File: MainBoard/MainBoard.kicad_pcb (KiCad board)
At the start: 2 copper layers, 55 x 50 mm, 18 parts, among them CN1 HC-FPC-05-09-22RLTAG, CN3 PJ-342, J1 1769, Q2 MMBT2222ALT1G, U1 V3S, U10 F35SQA512M-WWT, U11 XC6206P302MR_C5148691, U2 ESP32-MINI-1-H4, U3 SGTL5000XNAA3R2, U4 BQ27220YZFR, U5 10104110-0001LF, U6 EA3036C, U7 MT3608, U8 PCM1807PW, U9 BQ24074RGTR, X1 FC-12M32.768KHZ7PF20PPM, X2 X322524MOB4SI

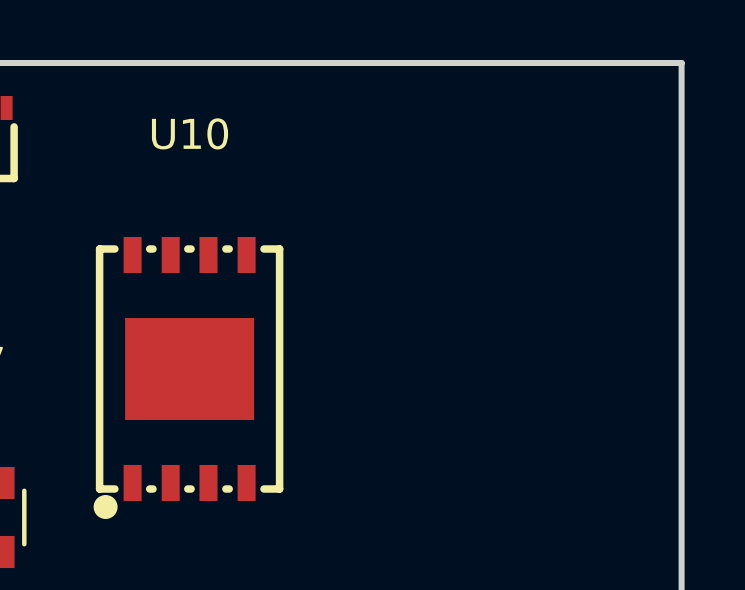
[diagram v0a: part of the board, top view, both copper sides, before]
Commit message: footprints for wheel + power changes for v3s
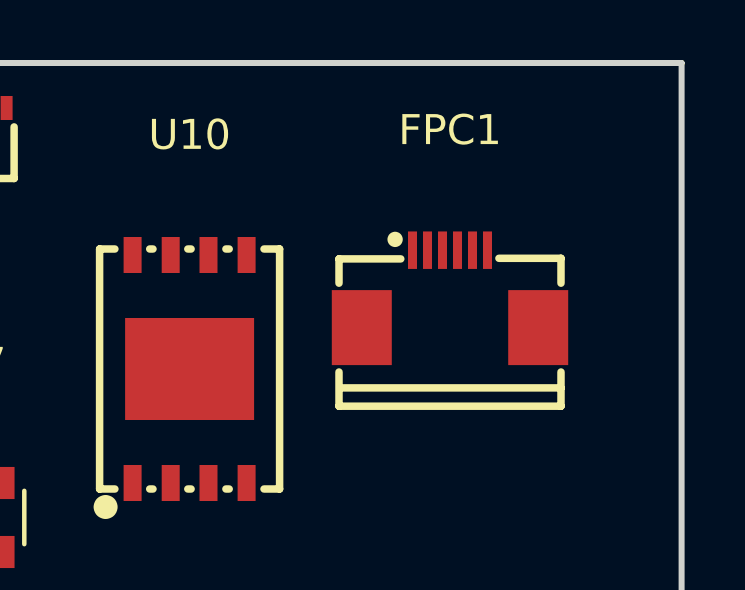
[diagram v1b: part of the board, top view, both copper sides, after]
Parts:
- added FPC1: FPC-05F-6PH20, easyeda2kicad:FPC-SMD_6P-P0.50_XUNPU_FPC-05F-6PH20, F.Cu at (169.8, 82.5)

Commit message: minor power changes
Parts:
- added C1: 10uF, Capacitor_SMD:C_0603_1608Metric, F.Cu at (182.2, 78.2)
- added C10: 220pF, Capacitor_SMD:C_0402_1005Metric, F.Cu at (181.6, 95.8)
- added C11: 220uF, Capacitor_SMD:C_1206_3216Metric, F.Cu at (203.7, 92.4)
- added C12: 220uF, Capacitor_SMD:C_1206_3216Metric, F.Cu at (203.7, 95.8)
- added C13: 1uF, Capacitor_SMD:C_0402_1005Metric, F.Cu at (202.3, 98.4)
- added C14: 1uF, Capacitor_SMD:C_0402_1005Metric, F.Cu at (202.3, 100.4)
- added C15: 0.1uF, Capacitor_SMD:C_0402_1005Metric, F.Cu at (198.3, 77.9)
- added C16: 0.1uF, Capacitor_SMD:C_0402_1005Metric, F.Cu at (202.3, 102.4)
- added C17: 10uF, Capacitor_SMD:C_0603_1608Metric, F.Cu at (186.2, 80.7)
- added C18: 0.1uF, Capacitor_SMD:C_0402_1005Metric, F.Cu at (205.1, 98.4)
- added C19: 0.1uF, Capacitor_SMD:C_0402_1005Metric, F.Cu at (181.6, 97.8)
- added C2: 10uF, Capacitor_SMD:C_0603_1608Metric, F.Cu at (182.2, 80.7)
- added C20: 0.1uF, Capacitor_SMD:C_0402_1005Metric, F.Cu at (205.1, 100.4)
- added C21: 0.1uF, Capacitor_SMD:C_0402_1005Metric, F.Cu at (205.1, 102.4)
- added C22: 0.1uF, Capacitor_SMD:C_0402_1005Metric, F.Cu at (208.0, 98.4)
- added C23: 0.1uF, Capacitor_SMD:C_0402_1005Metric, F.Cu at (208.0, 100.4)
- added C24: 0.1uF, Capacitor_SMD:C_0402_1005Metric, F.Cu at (208.0, 102.4)
- added C25: 1uF, Capacitor_SMD:C_0402_1005Metric, F.Cu at (181.6, 99.8)
- added C26: 4.7uF, Capacitor_SMD:C_0402_1005Metric, F.Cu at (181.6, 101.7)
- added C27: 4.7uF, Capacitor_SMD:C_0402_1005Metric, F.Cu at (184.5, 87.9)
- added C28: 22uF, Capacitor_SMD:C_0603_1608Metric, F.Cu at (186.2, 83.2)
- added C29: 22uF, Capacitor_SMD:C_0603_1608Metric, F.Cu at (186.2, 85.7)
- added C3: 10uF, Capacitor_SMD:C_0603_1608Metric, F.Cu at (182.2, 83.2)
- added C30: 0.1uF, Capacitor_SMD:C_0402_1005Metric, F.Cu at (212.9, 91.7)
- added C31: 0.1uF, Capacitor_SMD:C_0402_1005Metric, F.Cu at (212.9, 93.7)
- added C32: 1uF, Capacitor_SMD:C_0402_1005Metric, F.Cu at (212.9, 95.7)
- added C33: 0.1uF, Capacitor_SMD:C_0402_1005Metric, F.Cu at (212.9, 97.6)
- added C34: 0.1uF, Capacitor_SMD:C_0402_1005Metric, F.Cu at (198.3, 79.9)
- added C35: 0.1uF, Capacitor_SMD:C_0402_1005Metric, F.Cu at (212.9, 101.6)
- added C36: 0.1uF, Capacitor_SMD:C_0402_1005Metric, F.Cu at (198.3, 81.8)
- added C37: 0.1uF, Capacitor_SMD:C_0402_1005Metric, F.Cu at (198.3, 83.8)
- added C38: 15pF, Capacitor_SMD:C_0402_1005Metric, F.Cu at (198.3, 85.8)
- added C39: 15pF, Capacitor_SMD:C_0402_1005Metric, F.Cu at (198.3, 87.8)
- added C4: 1uF, Capacitor_SMD:C_0402_1005Metric, F.Cu at (181.6, 87.9)
- added C40: 1.0uF, Capacitor_SMD:C_0402_1005Metric, F.Cu at (184.5, 89.9)
- added C41: 1.0uF, Capacitor_SMD:C_0402_1005Metric, F.Cu at (184.5, 91.9)
- added C42: 0.1uF, Capacitor_SMD:C_0402_1005Metric, F.Cu at (201.1, 77.9)
- added C43: 18pF, Capacitor_SMD:C_0402_1005Metric, F.Cu at (201.1, 79.9)
- added C44: 0.1uF, Capacitor_SMD:C_0402_1005Metric, F.Cu at (201.1, 81.8)
- added C45: 10uF, Capacitor_SMD:C_0603_1608Metric, F.Cu at (207.4, 78.2)
- added C46: 4.7uF, Capacitor_SMD:C_0402_1005Metric, F.Cu at (201.1, 83.8)
- added C47: 0.1uF, Capacitor_SMD:C_0402_1005Metric, F.Cu at (201.1, 85.8)
- added C48: 0.1uF, Capacitor_SMD:C_0402_1005Metric, F.Cu at (201.1, 87.8)
- added C49: 18pF, Capacitor_SMD:C_0402_1005Metric, F.Cu at (204.0, 77.9)
- added C5: 220pF, Capacitor_SMD:C_0402_1005Metric, F.Cu at (181.6, 89.9)
- added C50: 2.2uF, Capacitor_SMD:C_0402_1005Metric, F.Cu at (184.5, 93.8)
- added C51: 1uF, Capacitor_SMD:C_0402_1005Metric, F.Cu at (184.5, 95.8)
- added C52: 10uF, Capacitor_SMD:C_0603_1608Metric, F.Cu at (198.8, 92.0)
- added C53: 10uF, Capacitor_SMD:C_0603_1608Metric, F.Cu at (198.8, 94.5)
- added C54: 10uF, Capacitor_SMD:C_0603_1608Metric, F.Cu at (198.8, 97.0)
- added C55: 0.1uF, Capacitor_SMD:C_0402_1005Metric, F.Cu at (184.5, 97.8)
- added C56: 0.1uF, Capacitor_SMD:C_0402_1005Metric, F.Cu at (184.5, 99.8)
- added C57: 0.1uF, Capacitor_SMD:C_0402_1005Metric, F.Cu at (184.5, 101.7)
- added C58: 10uF, Capacitor_SMD:C_0603_1608Metric, F.Cu at (190.2, 78.2)
- added C59: 0.1uF, Capacitor_SMD:C_0402_1005Metric, F.Cu at (187.4, 87.9)
- added C6: 10uF, Capacitor_SMD:C_0603_1608Metric, F.Cu at (182.2, 85.7)
- added C60: 0.1uF, Capacitor_SMD:C_0402_1005Metric, F.Cu at (187.4, 89.9)
- added C61: 0.1uF, Capacitor_SMD:C_0402_1005Metric, F.Cu at (187.4, 91.9)
- added C62: 10uF, Capacitor_SMD:C_0603_1608Metric, F.Cu at (190.2, 80.7)
- added C63: 0.1uF, Capacitor_SMD:C_0402_1005Metric, F.Cu at (187.4, 93.8)
- added C64: 0.1uF, Capacitor_SMD:C_0402_1005Metric, F.Cu at (187.4, 95.8)
- added C65: 0.1uF, Capacitor_SMD:C_0402_1005Metric, F.Cu at (187.4, 97.8)
- added C66: 10uF, Capacitor_SMD:C_0603_1608Metric, F.Cu at (190.2, 83.2)
- added C67: 0.1uF, Capacitor_SMD:C_0402_1005Metric, F.Cu at (187.4, 99.8)
- added C68: 0.1uF, Capacitor_SMD:C_0402_1005Metric, F.Cu at (187.4, 101.7)
- added C69: 0.1uF, Capacitor_SMD:C_0402_1005Metric, F.Cu at (190.2, 87.9)
- added C7: 10uF, Capacitor_SMD:C_0603_1608Metric, F.Cu at (186.2, 78.2)
- added C70: 0.1uF, Capacitor_SMD:C_0402_1005Metric, F.Cu at (190.2, 89.9)
- added C71: 0.1uF, Capacitor_SMD:C_0402_1005Metric, F.Cu at (190.2, 91.9)
- added C72: 0.1uF, Capacitor_SMD:C_0402_1005Metric, F.Cu at (190.2, 93.8)
- added C73: 0.1uF, Capacitor_SMD:C_0402_1005Metric, F.Cu at (190.2, 95.8)
- added C74: 0.1uF, Capacitor_SMD:C_0402_1005Metric, F.Cu at (190.2, 97.8)
- added C75: 0.1uF, Capacitor_SMD:C_0402_1005Metric, F.Cu at (204.0, 79.9)
- added C76: 10uF, Capacitor_SMD:C_0603_1608Metric, F.Cu at (190.2, 85.7)
- added C77: 0.1uF, Capacitor_SMD:C_0402_1005Metric, F.Cu at (190.2, 99.8)
- added C78: 10uF, Capacitor_SMD:C_0603_1608Metric, F.Cu at (207.4, 80.7)
- added C79: 0.1uF, Capacitor_SMD:C_0402_1005Metric, F.Cu at (204.0, 81.8)
- added C8: 220pF, Capacitor_SMD:C_0402_1005Metric, F.Cu at (181.6, 91.9)
- added C9: 10uF, Capacitor_SMD:C_0402_1005Metric, F.Cu at (181.6, 93.8)
- added D1: RED, LED_SMD:LED_0402_1005Metric, F.Cu at (193.4, 88.0)
- added D2: GREEN, LED_SMD:LED_0402_1005Metric, F.Cu at (193.4, 89.9)
- added D3: D, Diode_SMD:D_0603_1608Metric, F.Cu at (195.3, 117.6)
- added H1: MountingHole, MountingHole:MountingHole_2.2mm_M2, F.Cu at (175.0, 77.5)
- added H2: MountingHole, MountingHole:MountingHole_2.2mm_M2, F.Cu at (140.0, 77.5)
- added H3: MountingHole, MountingHole:MountingHole_2.2mm_M2, F.Cu at (160.0, 122.5)
- added H4: MountingHole, MountingHole:MountingHole_2.2mm_M2, F.Cu at (125.0, 107.5)
- added JP1: SolderJumper_2_Open, Jumper:SolderJumper-2_P1.3mm_Open_Pad1.0x1.5mm, F.Cu at (185.8, 110.3)
- added JP2: SolderJumper_2_Open, Jumper:SolderJumper-2_P1.3mm_Open_Pad1.0x1.5mm, F.Cu at (185.8, 113.8)
- added JP3: SolderJumper_2_Open, Jumper:SolderJumper-2_P1.3mm_Open_Pad1.0x1.5mm, F.Cu at (182.2, 118.4)
- added L1: 1.5uH, Inductor_SMD:L_0402_1005Metric, F.Cu at (193.1, 91.9)
- added L2: 1.5uH, Inductor_SMD:L_0402_1005Metric, F.Cu at (193.1, 93.9)
- added L3: 1.5uH, Inductor_SMD:L_0402_1005Metric, F.Cu at (193.1, 95.9)
- added L4: 4.7uH, Inductor_SMD:L_0402_1005Metric, F.Cu at (193.1, 97.9)
- added R1: 68K, Resistor_SMD:R_0402_1005Metric, F.Cu at (194.7, 109.4)
- added R10: 10K, Resistor_SMD:R_0402_1005Metric, F.Cu at (200.5, 111.4)
- added R11: 10K, Resistor_SMD:R_0402_1005Metric, F.Cu at (208.3, 109.4)
- added R12: 10K, Resistor_SMD:R_0402_1005Metric, F.Cu at (208.3, 111.4)
- added R13: 10K, Resistor_SMD:R_0402_1005Metric, F.Cu at (208.3, 113.3)
- added R14: 5.1K, Resistor_SMD:R_0402_1005Metric, F.Cu at (194.7, 121.9)
- added R15: 5.1K, Resistor_SMD:R_0402_1005Metric, F.Cu at (194.7, 123.9)
- added R16: 10K, Resistor_SMD:R_0402_1005Metric, F.Cu at (200.5, 113.3)
- added R17: 1K, Resistor_SMD:R_0402_1005Metric, F.Cu at (200.5, 115.3)
- added R18: 1K, Resistor_SMD:R_0402_1005Metric, F.Cu at (203.4, 109.4)
- added R19: 10K, Resistor_SMD:R_0402_1005Metric, F.Cu at (208.3, 115.3)
- added R2: 15K, Resistor_SMD:R_0402_1005Metric, F.Cu at (194.7, 111.4)
- added R20: 10K, Resistor_SMD:R_0402_1005Metric, F.Cu at (208.3, 117.3)
- added R21: 47K, Resistor_SMD:R_0402_1005Metric, F.Cu at (194.7, 125.9)
- added R22: 47K, Resistor_SMD:R_0402_1005Metric, F.Cu at (205.4, 121.9)
- added R23: 47K, Resistor_SMD:R_0402_1005Metric, F.Cu at (205.4, 123.9)
- added R24: 47K, Resistor_SMD:R_0402_1005Metric, F.Cu at (205.4, 125.9)
- added R25: 10K, Resistor_SMD:R_0402_1005Metric, F.Cu at (210.3, 121.9)
- added R26: 2K, Resistor_SMD:R_0402_1005Metric, F.Cu at (197.6, 121.9)
- added R27: 2K, Resistor_SMD:R_0402_1005Metric, F.Cu at (197.6, 123.9)
- added R28: 200K, Resistor_SMD:R_0402_1005Metric, F.Cu at (197.6, 125.9)
- added R29: 10M, Resistor_SMD:R_0402_1005Metric, F.Cu at (200.5, 121.9)
- added R3: 100K, Resistor_SMD:R_0402_1005Metric, F.Cu at (194.7, 113.3)
- added R30: 10K, Resistor_SMD:R_0402_1005Metric, F.Cu at (203.4, 111.4)
- added R31: 10K, Resistor_SMD:R_0402_1005Metric, F.Cu at (203.4, 113.3)
- added R32: 240, Resistor_SMD:R_0402_1005Metric, F.Cu at (200.5, 123.9)
- added R33: 10M, Resistor_SMD:R_0402_1005Metric, F.Cu at (203.4, 115.3)
- added R34: 10K, Resistor_SMD:R_0402_1005Metric, F.Cu at (200.5, 125.9)
- added R4: 200K, Resistor_SMD:R_0402_1005Metric, F.Cu at (194.7, 115.3)
- added R5: 100K, Resistor_SMD:R_0402_1005Metric, F.Cu at (197.6, 109.4)
- added R6: 100K, Resistor_SMD:R_0402_1005Metric, F.Cu at (197.6, 111.4)
- added R7: 1.13K, Resistor_SMD:R_0402_1005Metric, F.Cu at (197.6, 113.3)
- added R8: 1.18K, Resistor_SMD:R_0402_1005Metric, F.Cu at (197.6, 115.3)
- added R9: 73.3K, Resistor_SMD:R_0402_1005Metric, F.Cu at (200.5, 109.4)
- added TP1: TestPoint, TestPoint:TestPoint_Pad_1.5x1.5mm, F.Cu at (185.4, 121.9)
- added TP2: TestPoint, TestPoint:TestPoint_Pad_1.5x1.5mm, F.Cu at (185.4, 129.5)
- added TP3: TestPoint, TestPoint:TestPoint_Pad_1.5x1.5mm, F.Cu at (181.8, 110.3)
- added TP4: TestPoint, TestPoint:TestPoint_Pad_1.5x1.5mm, F.Cu at (181.8, 113.8)
- moved X2 61.0 mm to (165.7, 78.1), turned to 180 degrees
- moved U11 44.1 mm to (158.1, 111.1)
- moved FPC1 43.0 mm to (130.6, 100.3), turned to -90 degrees
- moved U9 34.3 mm to (160.4, 116.3)
- moved U6 34.1 mm to (165.5, 110.0)
- moved X1 29.9 mm to (143.5, 82.1), turned to 90 degrees
- moved U7 23.5 mm to (151.4, 113.5)
- moved Q2 22.5 mm to (160.3, 77.8)
- moved U10 19.6 mm to (170.8, 102.2), turned to 90 degrees
- moved Card1 13.2 mm to (170.0, 88.8)
- moved U1 12.5 mm to (152.4, 91.4)
- moved U8 9.50 mm to (140.9, 109.5), turned to -90 degrees
- moved CN1 2.48 mm to (151.2, 77.8)
- moved U4 2.07 mm to (170.9, 110.6)
- moved CN3 2.00 mm to (128.0, 118.0)
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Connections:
- CN3 pad 2: unconnected-(CN3-Pad2) -> GND
- CN3 pad 3: unconnected-(CN3-Pad3) -> GND
- FPC1 pad 1: unconnected-(FPC1-Pad1) -> +3.3V
- FPC1 pad 2: unconnected-(FPC1-Pad2) -> /BCD0
- FPC1 pad 3: unconnected-(FPC1-Pad3) -> /BCD1
- FPC1 pad 4: unconnected-(FPC1-Pad4) -> /BCD2
- FPC1 pad 5: unconnected-(FPC1-Pad5) -> /BCD3
- FPC1 pad 6: unconnected-(FPC1-Pad6) -> GND
- U1 pad 123: unconnected-(U1-HPVCCBP-Pad123) -> /HPVCCBP
- U1 pad 13: unconnected-(U1-PE18/CSI_D14/LCD_D20-Pad13) -> /BCD0
- U1 pad 14: unconnected-(U1-PE17/CSI_D13/LCD_D19-Pad14) -> /BCD1
- U1 pad 15: unconnected-(U1-PE16/CSI_D12/LCD_D18-Pad15) -> /BCD2
- U1 pad 16: unconnected-(U1-PE15/CSI_D11/LCD_D15-Pad16) -> /BCD3
- U1 pad 47: unconnected-(U1-VDD-CPU5-Pad47) -> +1V2
- U1 pad 8: /V3S-ESP32_RX -> V3S-ESP32_RX
- U1 pad 9: /V3S-ESP32_TX -> V3S-ESP32_TX
- U2 pad 25: /WiFi+BT/V3S-ESP32_TX -> V3S-ESP32_TX
- U2 pad 26: /WiFi+BT/V3S-ESP32_RX -> V3S-ESP32_RX
- U7 pad 4: unconnected-(U7-EN-Pad4) -> VSYS

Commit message: layout and starting routing
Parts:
- removed CN1: HC-FPC-05-09-22RLTAG, easyeda2kicad:CONN-SMD_22P-P0.50_HCTL_HC-FPC-05-09-22RLTAG
- removed Q2: MMBT2222ALT1G, easyeda2kicad:SOT-23-3_L2.9-W1.3-P1.90-LS2.4-BR
- removed U5: 10104110-0001LF, easyeda2kicad:MICRO-USB-SMD_AMPHENOL_10104110-0001LF
- added JP10: SolderJumper_2_Open, Jumper:SolderJumper-2_P1.3mm_Open_TrianglePad1.0x1.5mm, F.Cu at (135.7, 49.0)
- added JP11: SolderJumper_2_Open, Jumper:SolderJumper-2_P1.3mm_Open_TrianglePad1.0x1.5mm, F.Cu at (135.7, 52.5)
- added JP8: SolderJumper_2_Open, Jumper:SolderJumper-2_P1.3mm_Open_TrianglePad1.0x1.5mm, F.Cu at (135.7, 43.0)
- added JP9: SolderJumper_2_Open, Jumper:SolderJumper-2_P1.3mm_Open_TrianglePad1.0x1.5mm, F.Cu at (135.7, 46.0)
- added Q3: MMBT2222ALT1G, easyeda2kicad:SOT-23-3_L2.9-W1.3-P1.90-LS2.4-BR, F.Cu at (147.6, 66.2)
- added R42: 10K, Resistor_SMD:R_0402_1005Metric, F.Cu at (147.0, 46.5)
- added R43: 10, Resistor_SMD:R_0402_1005Metric, F.Cu at (147.5, 63.5)
- added SW1: TS3735A 250GF 030, easyeda2kicad:SW-SMD_4P-L3.7-W3.7-P2.70-LS3.7, B.Cu at (150.0, 98.2)
- added SW2: TS3735A 250GF 030, easyeda2kicad:SW-SMD_4P-L3.7-W3.7-P2.70-LS3.7, B.Cu at (165.0, 98.2)
- added SW3: TS3735A 250GF 030, easyeda2kicad:SW-SMD_4P-L3.7-W3.7-P2.70-LS3.7, B.Cu at (135.0, 98.2)
- added SW4: TS3735A 250GF 030, easyeda2kicad:SW-SMD_4P-L3.7-W3.7-P2.70-LS3.7, B.Cu at (150.0, 113.2)
- added SW5: TS3735A 250GF 030, easyeda2kicad:SW-SMD_4P-L3.7-W3.7-P2.70-LS3.7, B.Cu at (150.0, 83.2)
- added USB2: 105164-0001, easyeda2kicad:MICRO-USB-SMD_5P-P0.65-H-F_105164-0001, F.Cu at (150.0, 122.2)
- added X3: AFC01-S45FCA-00, easyeda2kicad:FPC-SMD_AFC01-S45FCA-00, F.Cu at (143.5, 55.2)
- C36, C37, C55, C76, C77, R26, R27: moved to B.Cu
- C9: footprint Capacitor_SMD:C_0402_1005Metric -> Capacitor_SMD:C_0603_1608Metric
- moved TP2 93.2 mm to (124.5, 59.0)
- moved R25 91.2 mm to (124.0, 92.5), turned to 90 degrees
- moved C30 90.1 mm to (123.5, 80.5), turned to 90 degrees
- moved C31 90.1 mm to (123.5, 82.5), turned to -90 degrees
- moved C32 87.0 mm to (126.0, 92.0)
- moved C33 86.4 mm to (126.5, 96.5)
- moved TP1 85.8 mm to (124.5, 61.5)
- moved R20 81.2 mm to (159.5, 52.5)
- moved C12 77.3 mm to (128.0, 111.5)
- moved R13 75.7 mm to (164.0, 52.0), turned to 180 degrees
- moved C22 75.4 mm to (135.0, 117.5), turned to 180 degrees
- moved C14 75.4 mm to (127.0, 104.0), turned to -90 degrees
- moved C11 74.6 mm to (134.5, 120.5), turned to -90 degrees
- moved C13 74.5 mm to (128.0, 104.0), turned to -90 degrees
- moved TP4 74.0 mm to (124.5, 67.0)
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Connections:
- U1 pad 1: unconnected-(U1-PG4/SDC1_D2/PG_EINT4-Pad1) -> /BCD0
- U1 pad 11: unconnected-(U1-PE19/CSI_D15/LCD_D21-Pad11) -> LCD_D21
- U1 pad 13: /BCD0 -> LCD_D20
- U1 pad 14: /BCD1 -> LCD_D19
- U1 pad 15: /BCD2 -> LCD_D18
- U1 pad 16: /BCD3 -> LCD_D15
- U1 pad 17: unconnected-(U1-PE14/CSI_D10/LCD_D14-Pad17) -> LCD_D14
- U1 pad 18: unconnected-(U1-PE13/CSI_D9/LCD_D13-Pad18) -> LCD_D13
- U1 pad 2: unconnected-(U1-PG3/SDC1_D1/PG_EINT3-Pad2) -> /BCD1
- U1 pad 22: unconnected-(U1-PE12/CSI_D8/LCD_D12-Pad22) -> LCD_D12
- U1 pad 23: unconnected-(U1-PE11/CSI_D7/LCD_D11-Pad23) -> LCD_D11
- U1 pad 24: unconnected-(U1-PE10/CSI_D6/LCD_D10-Pad24) -> LCD_D10
- U1 pad 27: unconnected-(U1-PE9/CSI_D5/LCD_D7-Pad27) -> LCD_D7
- U1 pad 28: unconnected-(U1-PE8/CSI_D4/LCD_D6-Pad28) -> LCD_D6
- U1 pad 3: unconnected-(U1-PG2/SDC1_D0/PG_EINT2-Pad3) -> /BCD2
- U1 pad 30: unconnected-(U1-PE7/CSI_D3/LCD_D5-Pad30) -> LCD_D5
- U1 pad 31: unconnected-(U1-PE6/CSI_D2/LCD_D4-Pad31) -> LCD_D4
- U1 pad 32: unconnected-(U1-PE5/CSI_D1/LCD_D3-Pad32) -> LCD_D3
- U1 pad 33: unconnected-(U1-PE4/CSI_D0/LCD_D2-Pad33) -> LCD_D2
- U1 pad 34: unconnected-(U1-PE3/CSI_VSYNC/LCD_VSYNC-Pad34) -> LCD_VSYNC
- U1 pad 35: GPOUT -> LCD_HSYNC
- U1 pad 36: LCD_CS -> LCD_DE
- U1 pad 37: PCM_CS -> LCD_CLK
- U1 pad 39: unconnected-(U1-PB0/UART2_TX/PB_EINT0-Pad39) -> GPOUT
- U1 pad 4: unconnected-(U1-PG1/SDC1_CMD/PG_EINT1-Pad4) -> /BCD3
- U1 pad 40: unconnected-(U1-PB1/UART2_RX/PB_EINT1-Pad40) -> LCD_CS
- U1 pad 42: unconnected-(U1-PB3/UART2_CTS/PB_EINT3-Pad42) -> PCM_CS
- U1 pad 6: unconnected-(U1-PE24/LCD_D23-Pad6) -> LCD_D23
- U1 pad 7: unconnected-(U1-PE23/LCD_D22-Pad7) -> LCD_D22
- U2 pad 10: unconnected-(U2-I35-Pad10) -> /WiFi+BT/IO35
- U2 pad 11: unconnected-(U2-IO32-Pad11) -> /WiFi+BT/IO32
- U2 pad 12: unconnected-(U2-IO33-Pad12) -> /WiFi+BT/IO33
- U2 pad 13: unconnected-(U2-IO25-Pad13) -> /WiFi+BT/IO25
- U2 pad 9: unconnected-(U2-I34-Pad9) -> /WiFi+BT/IO34
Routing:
- net /USB_D+: track 0.00 -> 43.6 mm, vias 0 -> 2
- net /USB_D-: track 0.00 -> 43.5 mm, vias 0 -> 2
- net LCD_D23: track 0.00 -> 32.3 mm
- net LCD_DE: track 0.00 -> 31.5 mm
- net LCD_D22: track 0.00 -> 31.5 mm
- net LCD_D21: track 0.00 -> 31.3 mm
- net LCD_D20: track 0.00 -> 30.8 mm
- net LCD_D19: track 0.00 -> 30.0 mm
- net LCD_D18: track 0.00 -> 29.2 mm
- net LCD_D15: track 0.00 -> 28.5 mm
- net LCD_D14: track 0.00 -> 27.8 mm
- net LCD_D13: track 0.00 -> 27.1 mm
- net LCD_D12: track 0.00 -> 26.9 mm
- net LCD_D11: track 0.00 -> 26.2 mm
- net LCD_D10: track 0.00 -> 25.3 mm
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- added copper zone on F.Cu, net GND
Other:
- board size 55 x 50 mm -> 55 x 90 mm

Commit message: starting to route
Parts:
- removed C74: 0.1uF, Capacitor_SMD:C_0402_1005Metric
- moved U10 46.3 mm to (150.2, 108.5)
- moved C35 46.3 mm to (144.8, 110.8)
- moved C9 33.5 mm to (174.5, 63.8), turned to 0 degrees
- moved R5 30.7 mm to (174.5, 66.8), turned to 90 degrees
- moved R6 30.5 mm to (173.5, 65.7), turned to -90 degrees
- moved C2 29.7 mm to (169.5, 63.0), turned to 90 degrees
- moved C10 29.5 mm to (172.5, 65.8), turned to -90 degrees
- moved L3 28.5 mm to (171.0, 65.2), turned to 180 degrees
- moved C1 28.0 mm to (168.0, 63.5), turned to 90 degrees
- moved R3 26.5 mm to (174.0, 71.2), turned to 180 degrees
- moved C8 24.9 mm to (172.0, 70.2), turned to 0 degrees
- moved U6 24.8 mm to (169.8, 67.8), turned to 90 degrees
- moved R4 24.1 mm to (172.0, 71.2), turned to 0 degrees
- moved L1 22.9 mm to (166.5, 66.8), turned to 0 degrees
- moved L2 22.8 mm to (170.5, 70.7), turned to 90 degrees
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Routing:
- net +3.3V: track 0.00 -> 57.4 mm, vias 0 -> 1
- net HPOUTL: track 0.00 -> 53.6 mm
- net HPOUTR: track 0.00 -> 51.7 mm
- net +1V2: track 0.00 -> 50.9 mm, vias 0 -> 1
- net SDC0_D2: track 0.00 -> 42.9 mm, vias 0 -> 2
- net SDC0_D3: track 0.00 -> 42.1 mm, vias 0 -> 2
- net SDC0_CMD: track 0.00 -> 41.6 mm, vias 0 -> 2
- net SDC0_D1: track 0.00 -> 40.9 mm, vias 0 -> 2
- net SDC0_CLK: track 0.00 -> 40.4 mm, vias 0 -> 2
- net SDC0_D0: track 0.00 -> 39.7 mm, vias 0 -> 2
- net SPI_MOSI: track 0.00 -> 39.1 mm, vias 0 -> 2
- net SPI_CLK: track 0.00 -> 36.6 mm
- net LCD_VSYNC: track 0.00 -> 35.6 mm, vias 0 -> 2
- net LCD_CLK: track 0.00 -> 35.0 mm
- net UART0_TX: track 0.00 -> 34.3 mm
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- added copper zone on F.Cu, net +1V8
- added copper zone on F.Cu, net +5V
- added copper zone on B.Cu, net GND

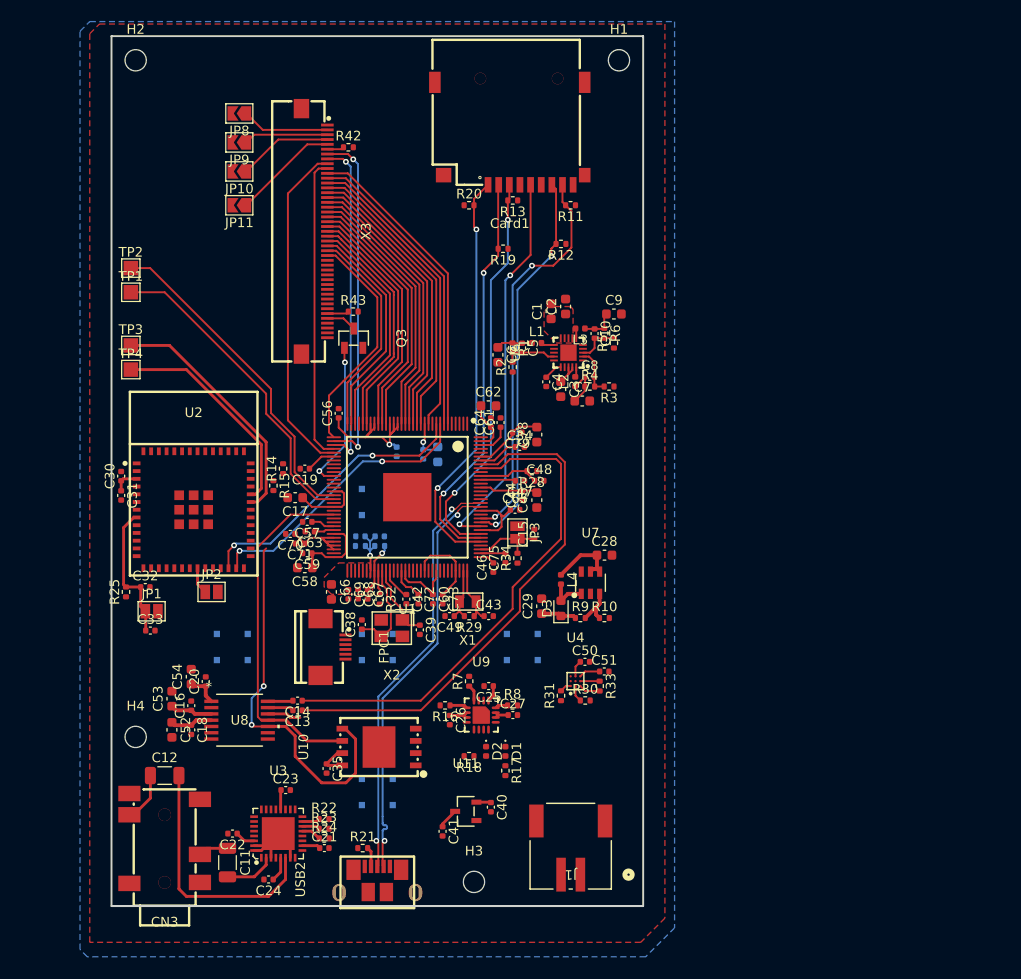
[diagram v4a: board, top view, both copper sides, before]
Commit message: routed signals
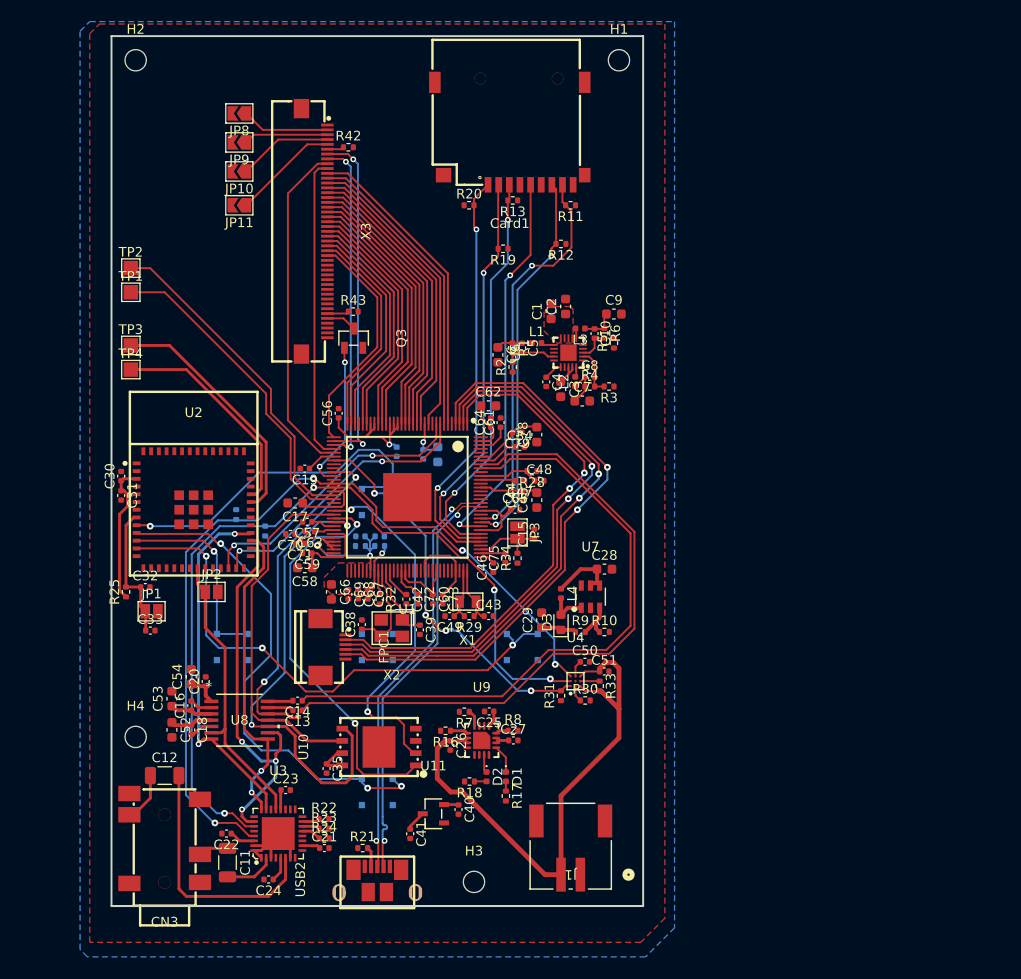
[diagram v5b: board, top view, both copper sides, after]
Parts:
- R14, R15: moved to B.Cu
- moved R14 6.79 mm to (135.4, 84.5)
- moved R15 4.78 mm to (138.4, 86.2)
- moved C40 3.36 mm to (158.4, 115.0)
- moved C41 3.36 mm to (153.4, 117.5)
- moved U11 3.36 mm to (155.8, 115.5)
- moved R7 3.20 mm to (159.0, 104.9), turned to 180 degrees
- moved C26 2.63 mm to (157.6, 108.4)
- moved D1 2.63 mm to (163.3, 111.6)
- moved D2 2.63 mm to (161.3, 111.6)
- moved R16 2.63 mm to (157.1, 106.9)
- moved R17 2.63 mm to (163.3, 113.6)
- moved U9 2.63 mm to (160.8, 107.9)
- moved C25 2.63 mm to (161.6, 104.9)
- moved C27 2.63 mm to (164.1, 107.9)
- moved R18 2.63 mm to (159.5, 112.1)
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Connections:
- U1 pad 40: LCD_CS -> unconnected-(U1-PB1/UART2_RX/PB_EINT1-Pad40)
- U1 pad 41: LCD_RST -> unconnected-(U1-PB2/UART2_RTS/PB_EINT2-Pad41)
- U1 pad 44: LCD_DC -> unconnected-(U1-PB5/PWM1/PB_EINT5-Pad44)
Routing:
- net I2C_SDA: track 0.00 -> 88.0 mm, vias 0 -> 4
- net I2C_SCK: track 0.00 -> 87.6 mm, vias 0 -> 4
- net /BCD3: track 0.00 -> 61.5 mm, vias 0 -> 2
- net /BCD2: track 0.00 -> 59.2 mm, vias 0 -> 2
- net /BCD1: track 0.00 -> 56.9 mm, vias 0 -> 2
- net /WiFi+BT/IO33: track 0.00 -> 56.3 mm, vias 0 -> 3
- net /BCD0: track 0.00 -> 54.6 mm, vias 0 -> 2
- net /WiFi+BT/IO35: track 0.00 -> 52.2 mm, vias 0 -> 3
- net +VBAT: track 6.67 -> 57.8 mm
- net NAND_CS: track 0.00 -> 42.1 mm, vias 0 -> 2
- net I2S_PCMOUT: track 0.00 -> 39.1 mm, vias 0 -> 3
- net GPOUT: track 1.21 -> 39.9 mm, vias 0 -> 4
- net I2S_WS: track 0.00 -> 37.1 mm, vias 0 -> 2
- net SPI_MISO: track 0.00 -> 36.8 mm, vias 0 -> 2
- net /WiFi+BT/IO34: track 0.00 -> 36.4 mm, vias 0 -> 1
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
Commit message: everything routed initial
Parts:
- C56: moved to B.Cu
- moved C56 3.70 mm to (149.3, 75.7)
- moved C37 2.72 mm to (150.8, 85.8), turned to 0 degrees
- moved C19 2.09 mm to (142.1, 77.7), turned to 90 degrees
- moved C17 1.26 mm to (140.3, 83.7)
- moved C57 1.25 mm to (141.5, 85.2)
- moved C55 1.10 mm to (152.0, 76.9), turned to 90 degrees
- moved C78 0.28 mm to (166.5, 76.5)
- moved C44 0.25 mm to (165.2, 82.5)
- moved R27 0.25 mm to (148.2, 88.0)
- moved C22 0.14 mm to (134.5, 117.4)
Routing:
- net +3.3V: track 69.5 -> 450.8 mm, vias 1 -> 20
- net +1V8: track 24.4 -> 147.1 mm, vias 1 -> 8
- net GND: track 17.9 -> 118.1 mm, vias 0 -> 76
- net +1V2: track 50.7 -> 132.3 mm, vias 1 -> 10
- net +5V: track 12.8 -> 94.0 mm, vias 0 -> 5
- net +3V0: track 11.1 -> 66.3 mm, vias 0 -> 4
- net VSYS: track 8.92 -> 48.1 mm, vias 0 -> 2
- net /WiFi+BT/IO25: track 0.00 -> 31.9 mm, vias 0 -> 3
- net VBUS: track 1.71 -> 23.5 mm, vias 0 -> 2
- net LCD_LIGHT: track 15.6 -> 21.1 mm
- net LCD_DE: track 31.5 -> 35.3 mm
- net NAND_CS: track 42.1 -> 45.8 mm
- net SPI_MISO: track 36.8 -> 40.3 mm
- net /WiFi+BT/IO35: track 52.2 -> 55.5 mm, vias 3 -> 4
- net LCD_CLK: track 35.0 -> 37.4 mm
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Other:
- outline, holes or cut-outs redrawn
